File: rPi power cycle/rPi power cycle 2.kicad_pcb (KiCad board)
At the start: 2 copper layers, 53.3 x 25.4 mm, 9 parts, among them J1 RPi GPIO, J2 BATT, J3 RPi PWR, Q1 BC548

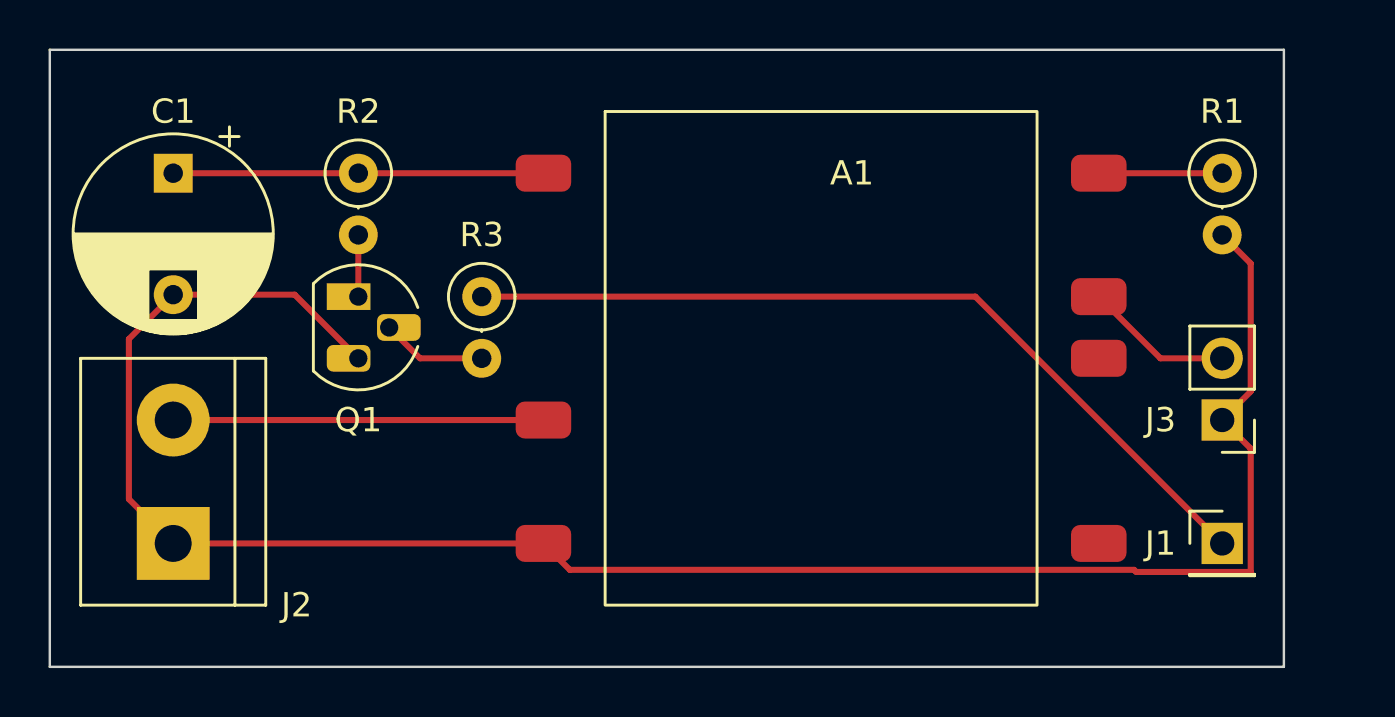
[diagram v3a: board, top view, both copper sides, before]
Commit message: Use via to simulate internal connections
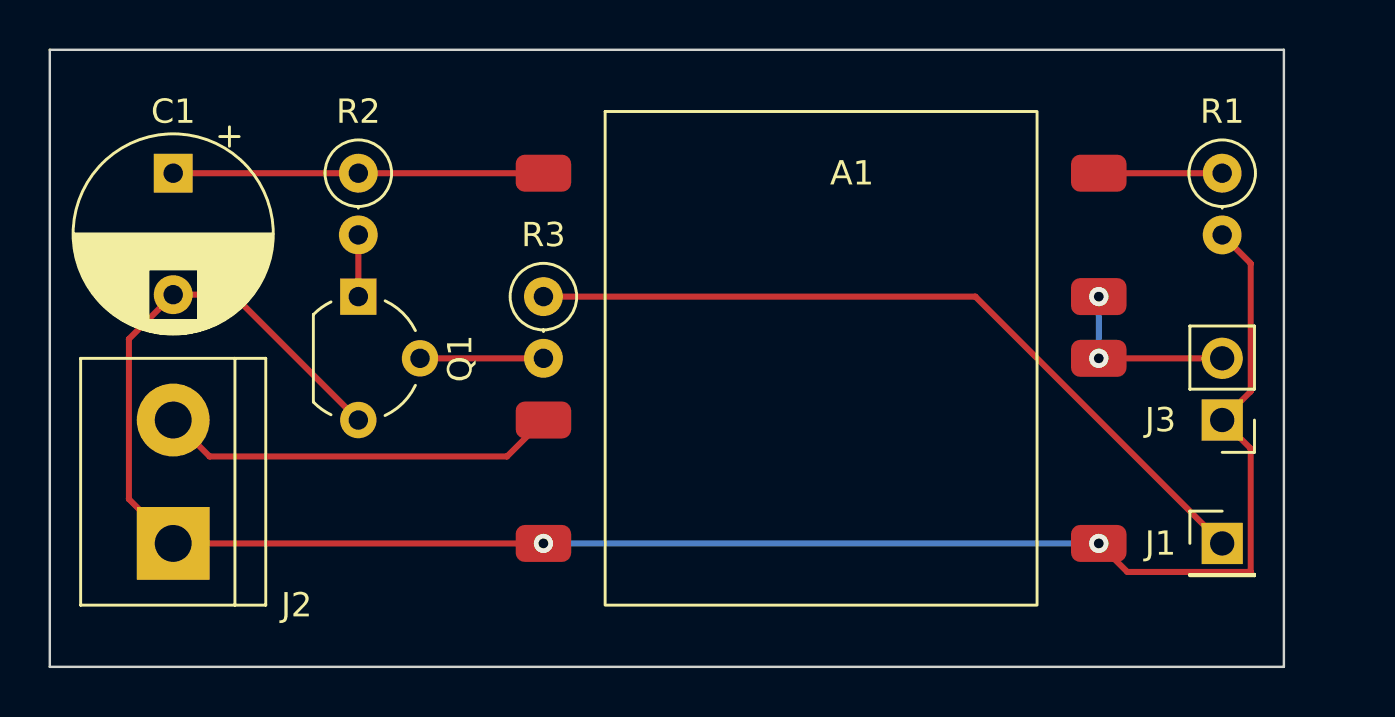
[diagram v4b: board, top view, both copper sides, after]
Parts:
- Q1: footprint Package_TO_SOT_THT:TO-92_HandSolder -> Package_TO_SOT_THT:TO-92_Wide
- moved R3 2.54 mm to (104.1, 86.4)
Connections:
- A1 pad 4: unconnected-(A1-Pad4) -> GND
- A1 pad 5: unconnected-(A1-Pad5) -> +5V
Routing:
- net Net-(J1-Pad1): track 34.7 -> 32.1 mm
- net +5V: track 6.13 -> 7.62 mm, vias 0 -> 2
- net +12V: track 15.2 -> 16.5 mm
- net GND: track 80.6 -> 81.7 mm, vias 0 -> 2
- net Net-(Q1-Pad2): track 4.34 -> 5.08 mm

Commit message: Move routing to back
Simulate perfboard connections
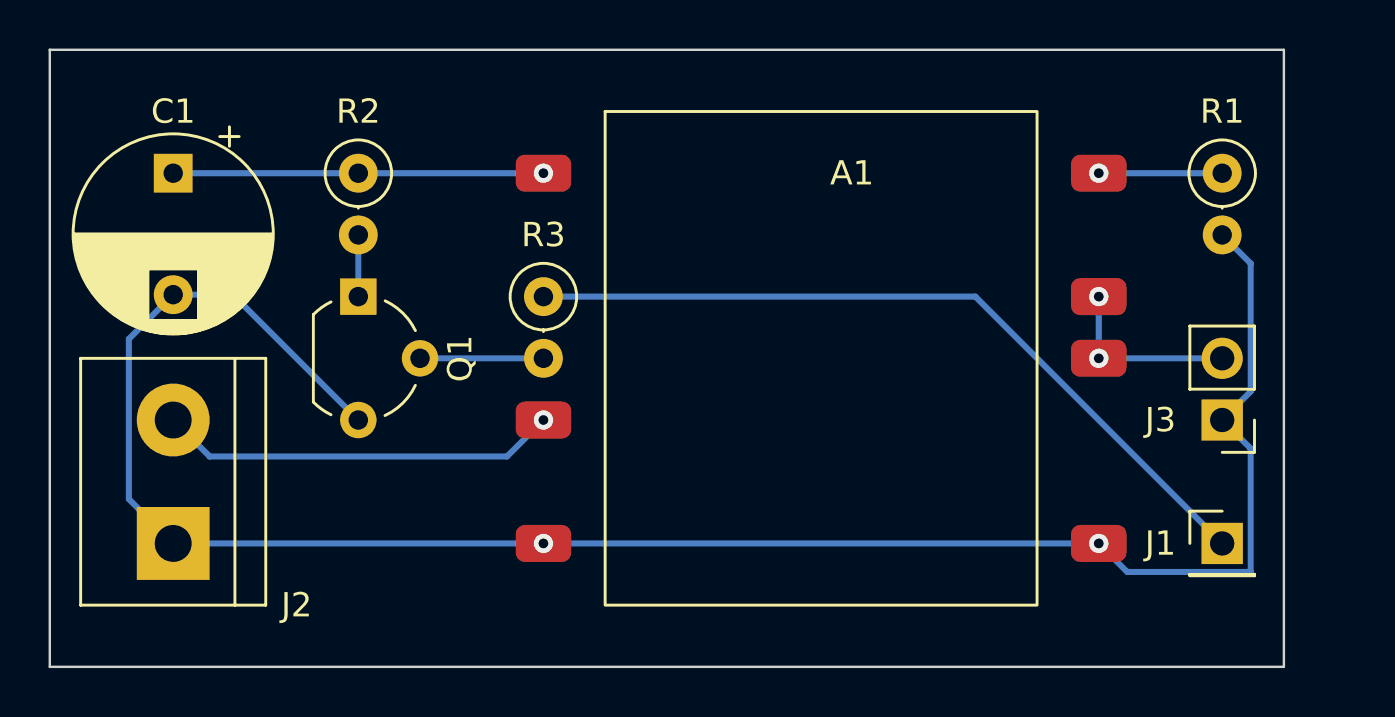
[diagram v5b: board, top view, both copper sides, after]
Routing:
- net Net-(A1-Pad7): vias 0 -> 1
- net Net-(A1-Pad1): vias 0 -> 1
- net +12V: vias 0 -> 1
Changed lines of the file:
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@@
   (gr_circle (center 137.16 81.28) (end 137.16 81.28) (layer "Edge.Cuts") (width 0.1) (fill none))
   (gr_rect (start 83.82 76.2) (end 134.62 101.6) (layer "Edge.Cuts") (width 0.1) (fill none))
-  (segment (start 88.9 81.28) (end 104.14 81.28) (width 0.25) (layer "F.Cu") (net 1))
-  (segment (start 90.4 92.94) (end 102.64 92.94) (width 0.25) (layer "F.Cu") (net 2))
-  (segment (start 88.9 91.44) (end 90.4 92.94) (width 0.25) (layer "F.Cu") (net 2))
-  (segment (start 102.64 92.94) (end 104.14 91.44) (width 0.25) (layer "F.Cu") (net 2))
-  (segment (start 88.9 96.52) (end 87.075489 94.695489) (width 0.25) (layer "F.Cu") (net 3))
-  (segment (start 128.174511 97.694511) (end 127 96.52) (width 0.25) (layer "F.Cu") (net 3))
-  (segment (start 132.08 91.44) (end 133.254511 90.265489) (width 0.25) (layer "F.Cu") (net 3))
-  (segment (start 88.9 96.52) (end 104.14 96.52) (width 0.25) (layer "F.Cu") (net 3))
-  (segment (start 133.254511 90.265489) (end 133.254511 84.994511) (width 0.25) (layer "F.Cu") (net 3))
-  (segment (start 91.36 86.28) (end 88.9 86.28) (width 0.25) (layer "F.Cu") (net 3))
-  (segment (start 133.254511 97.694511) (end 128.174511 97.694511) (width 0.25) (layer "F.Cu") (net 3))
-  (segment (start 133.254511 84.994511) (end 132.08 83.82) (width 0.25) (layer "F.Cu") (net 3))
-  (segment (start 133.254511 92.614511) (end 133.254511 97.694511) (width 0.25) (layer "F.Cu") (net 3))
-  (segment (start 87.075489 88.104511) (end 88.9 86.28) (width 0.25) (layer "F.Cu") (net 3))
-  (segment (start 96.52 91.44) (end 91.36 86.28) (width 0.25) (layer "F.Cu") (net 3))
-  (segment (start 132.08 91.44) (end 133.254511 92.614511) (width 0.25) (layer "F.Cu") (net 3))
-  (segment (start 87.075489 94.695489) (end 87.075489 88.104511) (width 0.25) (layer "F.Cu") (net 3))
+  (via (at 104.14 81.28) (size 0.8) (drill 0.4) (layers "F.Cu" "B.Cu") (net 1))
+  (segment (start 104.14 81.28) (end 88.9 81.28) (width 0.25) (layer "B.Cu") (net 1))
+  (via (at 104.14 91.44) (size 0.8) (drill 0.4) (layers "F.Cu" "B.Cu") (net 2))
+  (segment (start 88.9 91.44) (end 90.4 92.94) (width 0.25) (layer "B.Cu") (net 2))
+  (segment (start 90.4 92.94) (end 102.64 92.94) (width 0.25) (layer "B.Cu") (net 2))
+  (segment (start 102.64 92.94) (end 104.14 91.44) (width 0.25) (layer "B.Cu") (net 2))
   (via (at 104.14 96.52) (size 0.8) (drill 0.4) (layers "F.Cu" "B.Cu") (net 3))
   (via (at 127 96.52) (size 0.8) (drill 0.4) (layers "F.Cu" "B.Cu") (net 3))
+  (segment (start 127 96.52) (end 128.174511 97.694511) (width 0.25) (layer "B.Cu") (net 3))
+  (segment (start 88.9 86.28) (end 91.36 86.28) (width 0.25) (layer "B.Cu") (net 3))
+  (segment (start 133.254511 97.694511) (end 133.254511 92.614511) (width 0.25) (layer "B.Cu") (net 3))
+  (segment (start 133.254511 90.265489) (end 133.254511 84.994511) (width 0.25) (layer "B.Cu") (net 3))
+  (segment (start 88.9 96.52) (end 104.14 96.52) (width 0.25) (layer "B.Cu") (net 3))
   (segment (start 104.14 96.52) (end 127 96.52) (width 0.25) (layer "B.Cu") (net 3))
-  (segment (start 132.08 81.28) (end 127 81.28) (width 0.25) (layer "F.Cu") (net 4))
-  (segment (start 132.08 88.9) (end 127 88.9) (width 0.25) (layer "F.Cu") (net 5))
+  (segment (start 87.075489 88.104511) (end 88.9 86.28) (width 0.25) (layer "B.Cu") (net 3))
+  (segment (start 87.075489 94.695489) (end 87.075489 88.104511) (width 0.25) (layer "B.Cu") (net 3))
+  (segment (start 128.174511 97.694511) (end 133.254511 97.694511) (width 0.25) (layer "B.Cu") (net 3))
+  (segment (start 88.9 96.52) (end 87.075489 94.695489) (width 0.25) (layer "B.Cu") (net 3))
+  (segment (start 133.254511 84.994511) (end 132.08 83.82) (width 0.25) (layer "B.Cu") (net 3))
+  (segment (start 91.36 86.28) (end 96.52 91.44) (width 0.25) (layer "B.Cu") (net 3))
+  (segment (start 132.08 91.44) (end 133.254511 90.265489) (width 0.25) (layer "B.Cu") (net 3))
+  (segment (start 133.254511 92.614511) (end 132.08 91.44) (width 0.25) (layer "B.Cu") (net 3))
+  (via (at 127 81.28) (size 0.8) (drill 0.4) (layers "F.Cu" "B.Cu") (net 4))
+  (segment (start 127 81.28) (end 132.08 81.28) (width 0.25) (layer "B.Cu") (net 4))
   (via (at 127 88.9) (size 0.8) (drill 0.4) (layers "F.Cu" "B.Cu") (net 5))
   (via (at 127 86.36) (size 0.8) (drill 0.4) (layers "F.Cu" "B.Cu") (net 5))
+  (segment (start 127 88.9) (end 132.08 88.9) (width 0.25) (layer "B.Cu") (net 5))
   (segment (start 127 86.36) (end 127 88.9) (width 0.25) (layer "B.Cu") (net 5))
-  (segment (start 104.14 86.36) (end 121.92 86.36) (width 0.25) (layer "F.Cu") (net 6))
-  (segment (start 121.92 86.36) (end 132.08 96.52) (width 0.25) (layer "F.Cu") (net 6))
-  (segment (start 96.52 83.82) (end 96.52 86.36) (width 0.25) (layer "F.Cu") (net 7))
-  (segment (start 99.06 88.9) (end 104.14 88.9) (width 0.25) (layer "F.Cu") (net 8))
+  (segment (start 132.08 96.52) (end 121.92 86.36) (width 0.25) (layer "B.Cu") (net 6))
+  (segment (start 121.92 86.36) (end 104.14 86.36) (width 0.25) (layer "B.Cu") (net 6))
+  (segment (start 96.52 86.36) (end 96.52 83.82) (width 0.25) (layer "B.Cu") (net 7))
+  (segment (start 104.14 88.9) (end 99.06 88.9) (width 0.25) (layer "B.Cu") (net 8))
 )

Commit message: Add Power netclass and update track widths
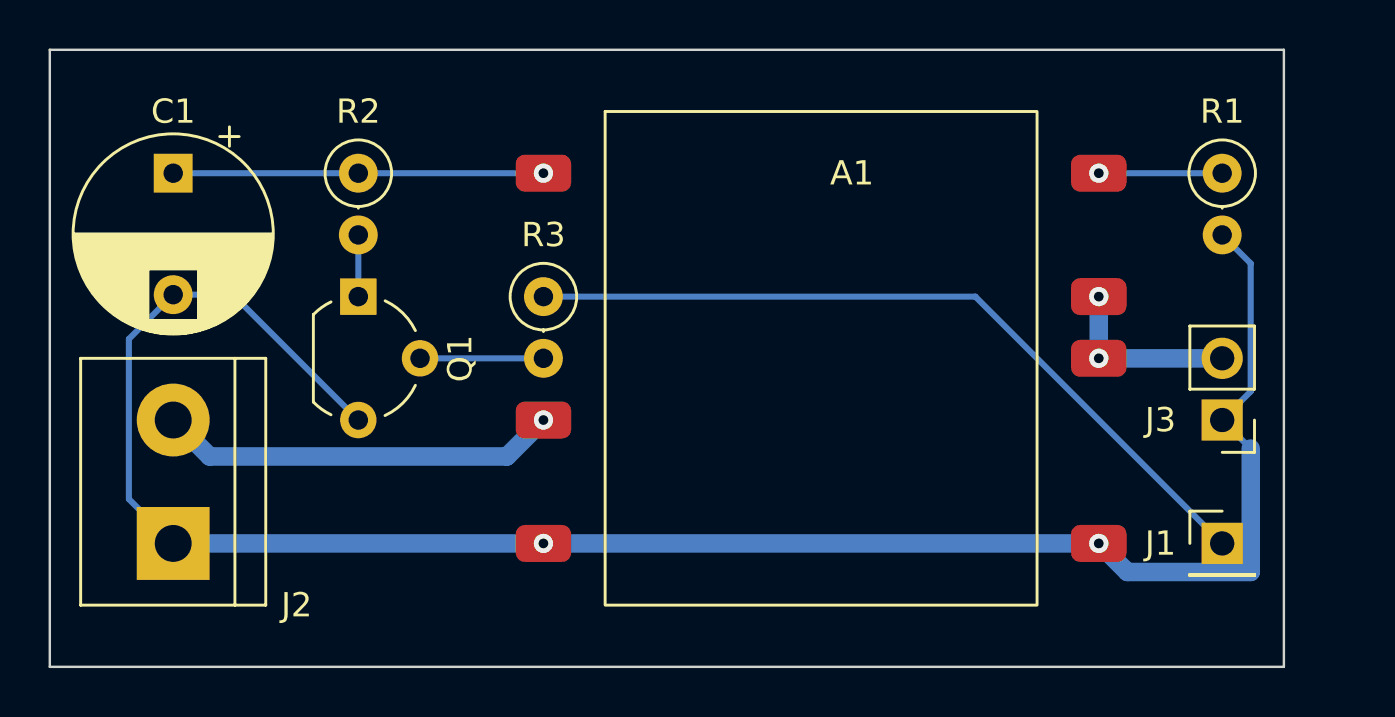
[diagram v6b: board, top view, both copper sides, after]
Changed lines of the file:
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@@
   )
   (setup
+    (stackup
+      (layer "F.SilkS" (type "Top Silk Screen"))
+      (layer "F.Paste" (type "Top Solder Paste"))
+      (layer "F.Mask" (type "Top Solder Mask") (thickness 0.01))
+      (layer "F.Cu" (type "copper") (thickness 0.035))
+      (layer "dielectric 1" (type "core") (thickness 1.51) (material "FR4") (epsilon_r 4.5) (loss_tangent 0.02))
+      (layer "B.Cu" (type "copper") (thickness 0.035))
+      (layer "B.Mask" (type "Bottom Solder Mask") (thickness 0.01))
+      (layer "B.Paste" (type "Bottom Solder Paste"))
+      (layer "B.SilkS" (type "Bottom Silk Screen"))
+      (copper_finish "None")
+      (dielectric_constraints no)
+    )
     (pad_to_mask_clearance 0)
     (pcbplotparams
@@
   (segment (start 104.14 81.28) (end 88.9 81.28) (width 0.25) (layer "B.Cu") (net 1))
   (via (at 104.14 91.44) (size 0.8) (drill 0.4) (layers "F.Cu" "B.Cu") (net 2))
-  (segment (start 88.9 91.44) (end 90.4 92.94) (width 0.25) (layer "B.Cu") (net 2))
-  (segment (start 90.4 92.94) (end 102.64 92.94) (width 0.25) (layer "B.Cu") (net 2))
-  (segment (start 102.64 92.94) (end 104.14 91.44) (width 0.25) (layer "B.Cu") (net 2))
+  (segment (start 88.9 91.44) (end 90.4 92.94) (width 0.762) (layer "B.Cu") (net 2))
+  (segment (start 90.4 92.94) (end 102.64 92.94) (width 0.762) (layer "B.Cu") (net 2))
+  (segment (start 102.64 92.94) (end 104.14 91.44) (width 0.762) (layer "B.Cu") (net 2))
   (via (at 104.14 96.52) (size 0.8) (drill 0.4) (layers "F.Cu" "B.Cu") (net 3))
   (via (at 127 96.52) (size 0.8) (drill 0.4) (layers "F.Cu" "B.Cu") (net 3))
-  (segment (start 127 96.52) (end 128.174511 97.694511) (width 0.25) (layer "B.Cu") (net 3))
+  (segment (start 127 96.52) (end 128.174511 97.694511) (width 0.762) (layer "B.Cu") (net 3))
   (segment (start 88.9 86.28) (end 91.36 86.28) (width 0.25) (layer "B.Cu") (net 3))
-  (segment (start 133.254511 97.694511) (end 133.254511 92.614511) (width 0.25) (layer "B.Cu") (net 3))
+  (segment (start 133.254511 97.694511) (end 133.254511 92.614511) (width 0.762) (layer "B.Cu") (net 3))
   (segment (start 133.254511 90.265489) (end 133.254511 84.994511) (width 0.25) (layer "B.Cu") (net 3))
-  (segment (start 88.9 96.52) (end 104.14 96.52) (width 0.25) (layer "B.Cu") (net 3))
-  (segment (start 104.14 96.52) (end 127 96.52) (width 0.25) (layer "B.Cu") (net 3))
+  (segment (start 88.9 96.52) (end 104.14 96.52) (width 0.762) (layer "B.Cu") (net 3))
+  (segment (start 104.14 96.52) (end 127 96.52) (width 0.762) (layer "B.Cu") (net 3))
   (segment (start 87.075489 88.104511) (end 88.9 86.28) (width 0.25) (layer "B.Cu") (net 3))
   (segment (start 87.075489 94.695489) (end 87.075489 88.104511) (width 0.25) (layer "B.Cu") (net 3))
-  (segment (start 128.174511 97.694511) (end 133.254511 97.694511) (width 0.25) (layer "B.Cu") (net 3))
+  (segment (start 128.174511 97.694511) (end 133.254511 97.694511) (width 0.762) (layer "B.Cu") (net 3))
   (segment (start 88.9 96.52) (end 87.075489 94.695489) (width 0.25) (layer "B.Cu") (net 3))
   (segment (start 133.254511 84.994511) (end 132.08 83.82) (width 0.25) (layer "B.Cu") (net 3))
@@
   (via (at 127 88.9) (size 0.8) (drill 0.4) (layers "F.Cu" "B.Cu") (net 5))
   (via (at 127 86.36) (size 0.8) (drill 0.4) (layers "F.Cu" "B.Cu") (net 5))
-  (segment (start 127 88.9) (end 132.08 88.9) (width 0.25) (layer "B.Cu") (net 5))
-  (segment (start 127 86.36) (end 127 88.9) (width 0.25) (layer "B.Cu") (net 5))
+  (segment (start 127 88.9) (end 132.08 88.9) (width 0.762) (layer "B.Cu") (net 5))
+  (segment (start 127 86.36) (end 127 88.9) (width 0.762) (layer "B.Cu") (net 5))
   (segment (start 132.08 96.52) (end 121.92 86.36) (width 0.25) (layer "B.Cu") (net 6))
   (segment (start 121.92 86.36) (end 104.14 86.36) (width 0.25) (layer "B.Cu") (net 6))
